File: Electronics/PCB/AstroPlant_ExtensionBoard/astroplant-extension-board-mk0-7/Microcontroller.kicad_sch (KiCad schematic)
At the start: 42 parts, among them J12 CONUFL001-SMD-T, J15 ZX62D-B-5PA8_30_, SW3 SW_Push, U1 USBLC6-2SC6, U2 STM32WB55RGVx

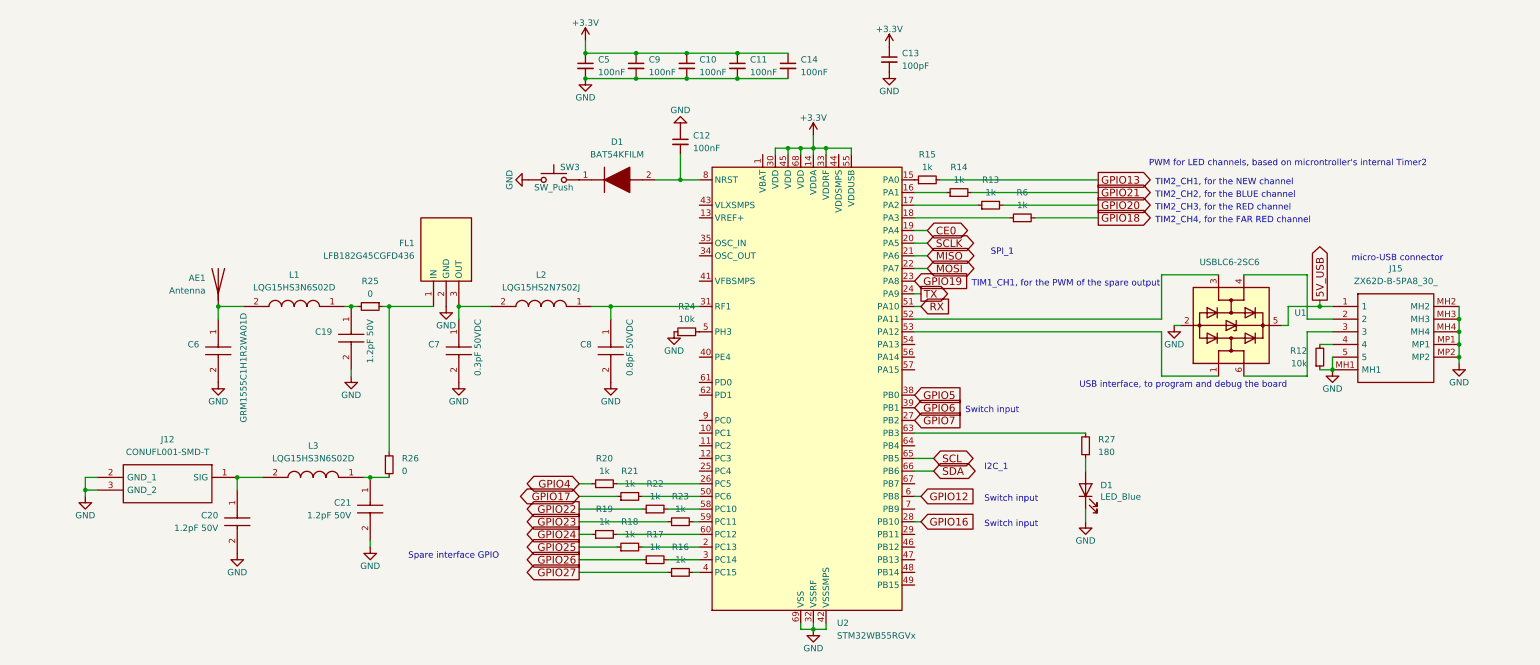
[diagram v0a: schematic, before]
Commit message: Updated PCB from a backup save, solve issues of the 1st prototype
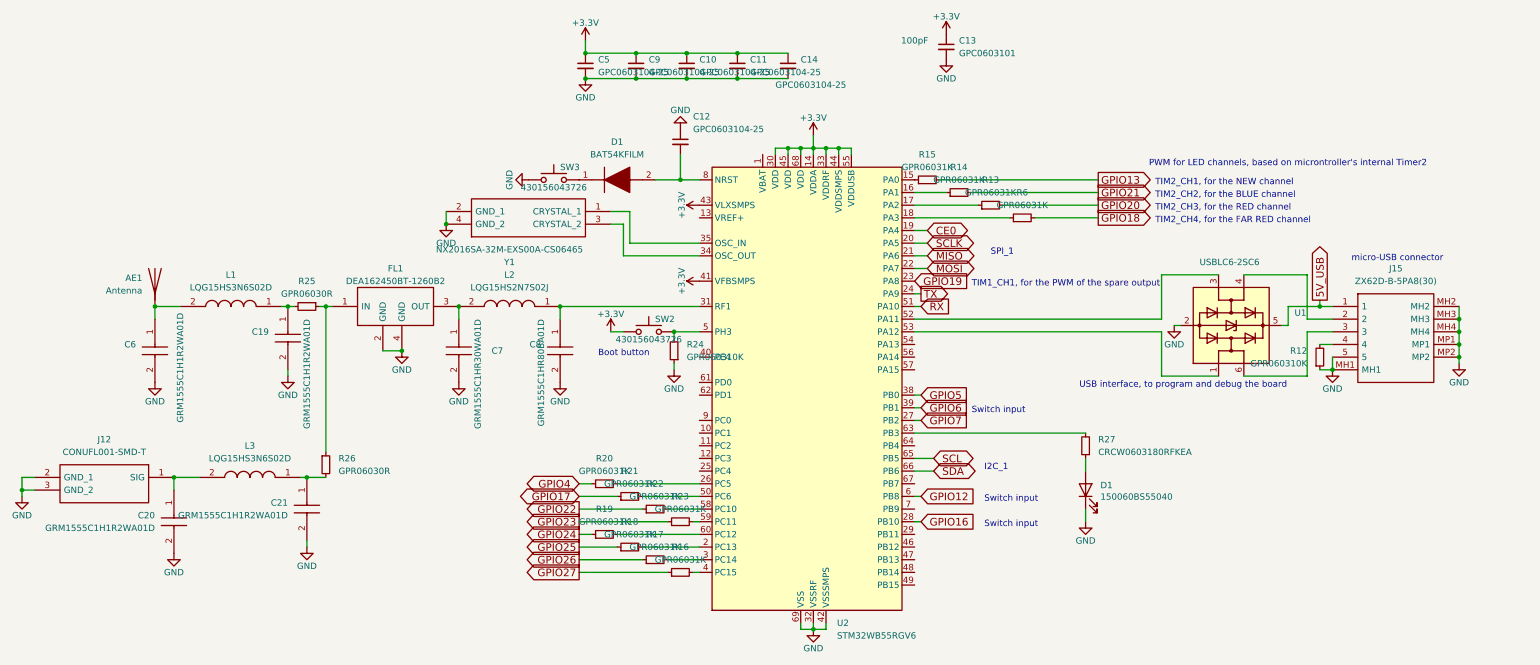
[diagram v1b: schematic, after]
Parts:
- removed FL1: LFB182G45CGFD436, SamacSys_Parts:LFB182G45CGFD436, symbol SamacSys_Parts:LFB182G45CGFD436
- added FL1: DEA162450BT-1260B2, DEA162450BT1295A1, symbol SamacSys_Parts:DEA162450BT-1260B2
- added SW2: 430156043726, Button_Switch_THT:SW_PUSH_6mm, symbol Astroplant_VFR-rescue:SW_Push-Astroplant_VFR-rescue-Astroplant_VFR-rescue
- added Y1: NX2016SA-32M-EXS00A-CS06465, NX2016SA32MEXS00ACS06465, symbol SamacSys_Parts:NX2016SA-32M-EXS00A-CS06465
- C10, C11, C12, C14, C5, C9: value 100nF -> GPC0603104-25; Capacitance (none) -> 100nF; MPN VJ0603Y104MXJCW1BC -> GPC0603104-25
- C13: value 100pF -> GPC0603101; Capacitance (none) -> 100pF; MPN VJ0603Y101KXQPW1BC -> GPC0603101; Manufacturer_Part_Number (none) -> GPC0603101
- C19, C20, C21: value 1.2pF 50V -> GRM1555C1H1R2WA01D; Capacitance (none) -> 0.8pF
- C6: Capacitance (none) -> 0.8pF
- C7: value 0.3pF 50VDC -> GRM1555C1HR30WA01D; Capacitance (none) -> 0.3pF
- C8: value 0.8pF 50VDC -> GRM1555C1HR80BA01D; Capacitance (none) -> 1.2pF
- D1: value LED_Blue -> 150060BS55040; MPN SMLEN3BC8TT86 -> 150060BS55040; Manufacturer_Part_Number (none) -> 150060BS55040
- J15: value ZX62D-B-5PA8_30_ -> ZX62D-B-5PA8(30); MPN (none) -> ZX62D-B-5PA8(30)
- R12, R24: value 10k -> GPR060310K; MPN CRCW060310K0DHEAP -> GPR060310K
- R13, R14, R15, R16, R17, R18, R19, R20, R21, R22, R23, R6: value 1k -> GPR06031K; MPN CRCW06031K00DHEBP -> GPR06031K
- R25, R26: value 0 -> GPR06030R; MPN CRCW04020000Z0EDC -> GPR06030R
- R27: value 180 -> CRCW0603180RFKEA
- SW3: value SW_Push -> 430156043726
- U2: value STM32WB55RGVx -> STM32WB55RGV6; MPN STM32WB55RGVx -> STM32WB55RGV6
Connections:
- net +3V3: now also U2.41 (VFBSMPS), U2.43 (VLXSMPS), U2.44 (VDDSMPS), SW2.1
- net GND: now also FL1.2 (GND), FL1.4 (GND), Y1.2 (GND_1), Y1.4 (GND_2)
- net at R25.1, R26.1: now also FL1.1 (IN)
- net at C7.1, L2.2: now also FL1.3 (OUT)
- net at R24.2, U2.5 (PH3): now also SW2.2
- net at U2.34 (OSC_OUT): now also Y1.3 (CRYSTAL_2)
- net at U2.35 (OSC_IN): now also Y1.1 (CRYSTAL_1)
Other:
- note added: "Boot button"
- note removed: "Spare interface GPIO"
- moved on the sheet: AE1, C13, C19, C20, C21, C6, C8, J12, L1, L2, L3, R24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
